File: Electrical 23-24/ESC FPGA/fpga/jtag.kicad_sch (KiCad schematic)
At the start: 0 parts

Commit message: idk but something
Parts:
- added J1: SBH11-PBPC-D07-ST-BK, programmer:SULLINS_SBH11-PBPC-D07-ST-BK, symbol programmer:SBH11-PBPC-D07-ST-BK
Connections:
- new net GND: J1.1, J1.11, J1.13, J1.3, J1.5, J1.7, J1.9
- new net TCK: J1.6
- new net TDI: J1.10
- new net TDO: J1.8
- new net TMS: J1.4
- new net VREF: J1.2
- no-connect marks 0 -> 2
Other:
- note added: "Due to the need of a programmer, it was decided that it was better to make one externally than on-board the chip This board includes a 14-pin 2.54mm header (the Xilinx Header is 2.00mm pitch)"
- note removed: "Due to the need of a programmer, it was decided that it was better to make one externally than on-board the chip"
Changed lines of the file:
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@@
 (kicad_sch (version 20230121) (generator eeschema)
   (paper "A4")
-  (text "Due to the need of a programmer, it was decided that it\nwas better to make one externally than on-board the chip"
-    (at 19.05 26.67 0)
+  (junction (at 127 91.44) (diameter 0) (color 0 0 0 0)
+  )
+  (junction (at 127 96.52) (diameter 0) (color 0 0 0 0)
+  )
+  (junction (at 127 104.14) (diameter 0) (color 0 0 0 0)
+  )
+  (junction (at 127 99.06) (diameter 0) (color 0 0 0 0)
+  )
+  (junction (at 127 101.6) (diameter 0) (color 0 0 0 0)
+  )
+  (junction (at 127 93.98) (diameter 0) (color 0 0 0 0)
+  )
+  (no_connect (at 152.4 101.6))
+  (no_connect (at 152.4 104.14))
+  (wire (pts (xy 127 91.44) (xy 127 93.98))
+    (stroke (width 0) (type default))
+  )
+  (wire (pts (xy 127 96.52) (xy 127 99.06))
+    (stroke (width 0) (type default))
+  )
+  (wire (pts (xy 127 88.9) (xy 127 91.44))
+    (stroke (width 0) (type default))
+  )
+  (wire (pts (xy 127 101.6) (xy 127 104.14))
+    (stroke (width 0) (type default))
+  )
+  (wire (pts (xy 127 93.98) (xy 127 96.52))
+    (stroke (width 0) (type default))
+  )
+  (wire (pts (xy 127 104.14) (xy 127 105.41))
+    (stroke (width 0) (type default))
+  )
+  (wire (pts (xy 127 99.06) (xy 127 101.6))
+    (stroke (width 0) (type default))
+  )
+  (text "Due to the need of a programmer, it was decided that it\nwas better to make one externally than on-board the chip\n\nThis board includes a 14-pin 2.54mm header\n(the Xilinx Header is 2.00mm pitch)"
+    (at 19.05 36.83 0)
     (effects (font (size 2.54 2.54)) (justify left bottom))
   )
+  (global_label "TDO" (shape input) (at 152.4 96.52 0) (fields_autoplaced)
+    (effects (font (size 1.27 1.27)) (justify left))
+    (property "Intersheetrefs" "${INTERSHEET_REFS}" (at 158.9533 96.52 0)
+      (effects (font (size 1.27 1.27)) (justify left) hide)
+    )
+  )
+  (global_label "VREF" (shape input) (at 152.4 88.9 0) (fields_autoplaced)
+    (effects (font (size 1.27 1.27)) (justify left))
+    (property "Intersheetrefs" "${INTERSHEET_REFS}" (at 159.9814 88.9 0)
+      (effects (font (size 1.27 1.27)) (justify left) hide)
+    )
+  )
+  (global_label "TMS" (shape input) (at 152.4 91.44 0) (fields_autoplaced)
+    (effects (font (size 1.27 1.27)) (justify left))
+    (property "Intersheetrefs" "${INTERSHEET_REFS}" (at 159.0137 91.44 0)
+      (effects (font (size 1.27 1.27)) (justify left) hide)
+    )
+  )
+  (global_label "TCK" (shape input) (at 152.4 93.98 0) (fields_autoplaced)
+    (effects (font (size 1.27 1.27)) (justify left))
+    (property "Intersheetrefs" "${INTERSHEET_REFS}" (at 158.8928 93.98 0)
+      (effects (font (size 1.27 1.27)) (justify left) hide)
+    )
+  )
+  (global_label "TDI" (shape input) (at 152.4 99.06 0) (fields_autoplaced)
+    (effects (font (size 1.27 1.27)) (justify left))
+    (property "Intersheetrefs" "${INTERSHEET_REFS}" (at 158.2276 99.06 0)
+      (effects (font (size 1.27 1.27)) (justify left) hide)
+    )
+  )
+  (symbol (lib_id "programmer:SBH11-PBPC-D07-ST-BK") (at 139.7 96.52 0) (unit 1)
+    (in_bom yes) (on_board yes) (dnp no) (fields_autoplaced)
+    (property "Reference" "J1" (at 139.7 81.28 0)
+      (effects (font (size 1.27 1.27)))
+    )
+    (property "Value" "SBH11-PBPC-D07-ST-BK" (at 139.7 83.82 0)
+      (effects (font (size 1.27 1.27)))
+    )
+    (property "Footprint" "programmer:SULLINS_SBH11-PBPC-D07-ST-BK" (at 139.7 96.52 0)
+      (effects (font (size 1.27 1.27)) (justify bottom) hide)
+    )
+    (property "Datasheet" "" (at 139.7 96.52 0)
+      (effects (font (size 1.27 1.27)) hide)
+    )
+    (property "PARTREV" "J" (at 139.7 96.52 0)
+      (effects (font (size 1.27 1.27)) (justify bottom) hide)
+    )
+    (property "STANDARD" "Manufacturer Recommendation" (at 139.7 96.52 0)
+      (effects (font (size 1.27 1.27)) (justify bottom) hide)
+    )
+    (property "MANUFACTURER" "Sullins" (at 139.7 96.52 0)
+      (effects (font (size 1.27 1.27)) (justify bottom) hide)
+    )
+    (pin "1")
+    (pin "10")
+    (pin "11")
+    (pin "12")
+    (pin "13")
+    (pin "14")
+    (pin "2")
+    (pin "3")
+    (pin "4")
+    (pin "5")
+    (pin "6")
+    (pin "7")
+    (pin "8")
+    (pin "9")
+    (instances
+      (project "fpga"
+        (path "/5bf59577-a814-4364-8f7a-37815cfb5474/3d3d8e49-9c73-4011-93e8-c0355c1f458a"
+          (reference "J1") (unit 1)
+        )
+      )
+    )
+  )
+  (symbol (lib_id "power:GND") (at 127 105.41 0) (unit 1)
+    (in_bom yes) (on_board yes) (dnp no) (fields_autoplaced)
+    (property "Reference" "#PWR09" (at 127 111.76 0)
+      (effects (font (size 1.27 1.27)) hide)
+    )
+    (property "Value" "GND" (at 127 110.49 0)
+      (effects (font (size 1.27 1.27)))
+    )
+    (property "Footprint" "" (at 127 105.41 0)
+      (effects (font (size 1.27 1.27)) hide)
+    )
+    (property "Datasheet" "" (at 127 105.41 0)
+      (effects (font (size 1.27 1.27)) hide)
+    )
+    (pin "1")
+    (instances
+      (project "fpga"
+        (path "/5bf59577-a814-4364-8f7a-37815cfb5474/3d3d8e49-9c73-4011-93e8-c0355c1f458a"
+          (reference "#PWR09") (unit 1)
+        )
+      )
+    )
+  )
 )

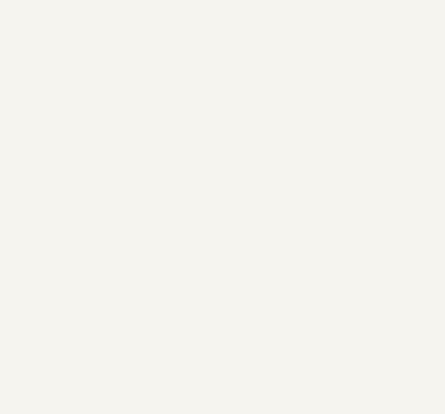
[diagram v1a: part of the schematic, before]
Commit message: Add fpga stuff and stencils
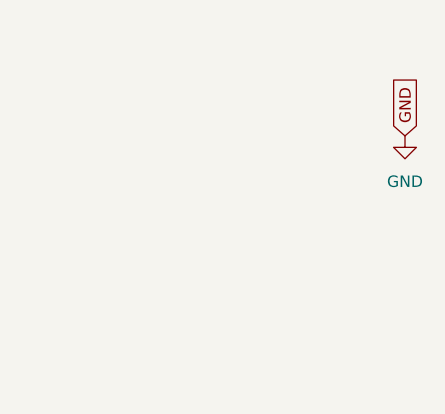
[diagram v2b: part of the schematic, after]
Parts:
- J1: Digi (none) -> https://www.digikey.com/en/products/detail/sullins-connecto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
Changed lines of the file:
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@@
+    )
+  )
+  (global_label "GND" (shape input) (at 273.05 29.21 90) (fields_autoplaced)
+    (effects (font (size 1.27 1.27)) (justify left))
+    (property "Intersheetrefs" "${INTERSHEET_REFS}" (at 273.05 22.3543 90)
+      (effects (font (size 1.27 1.27)) (justify left) hide)
     )
   )
@@
     )
   )
+  (symbol (lib_id "power:GND") (at 273.05 29.21 0) (unit 1)
+    (in_bom yes) (on_board yes) (dnp no) (fields_autoplaced)
+    (property "Reference" "#PWR016" (at 273.05 35.56 0)
+      (effects (font (size 1.27 1.27)) hide)
+    )
+    (property "Value" "GND" (at 273.05 34.29 0)
+      (effects (font (size 1.27 1.27)))
+    )
+    (property "Footprint" "" (at 273.05 29.21 0)
+      (effects (font (size 1.27 1.27)) hide)
+    )
+    (property "Datasheet" "" (at 273.05 29.21 0)
+      (effects (font (size 1.27 1.27)) hide)
+    )
+    (pin "1")
+    (instances
+      (project "fpga"
+        (path "/5bf59577-a814-4364-8f7a-37815cfb5474/3e04db34-3f8a-4742-be82-6fa24c009343"
+          (reference "#PWR016") (unit 1)
+        )
+        (path "/5bf59577-a814-4364-8f7a-37815cfb5474/1f83b38b-56ef-4110-879b-13379f9dd920"
+          (reference "#PWR026") (unit 1)
+        )
+        (path "/5bf59577-a814-4364-8f7a-37815cfb5474/a286b274-4434-47ab-983d-e64806fdcbd6"
+          (reference "#PWR036") (unit 1)
+        )
+        (path "/5bf59577-a814-4364-8f7a-37815cfb5474/3d3d8e49-9c73-4011-93e8-c0355c1f458a"
+          (reference "#PWR042") (unit 1)
+        )
+      )
+    )
+  )
   (symbol (lib_id "programmer:SBH11-PBPC-D07-ST-BK") (at 139.7 96.52 0) (unit 1)
     (in_bom yes) (on_board yes) (dnp no) (fields_autoplaced)
@@
       (effects (font (size 1.27 1.27)) (justify bottom) hide)
     )
+    (property "Digi" "https://www.digikey.com/en/products/detail/sullins-connector-solutions/sbh11-pbpc-d07-st-bk/1990063" (at 139.7 96.52 0)
+      (effects (font (size 1.27 1.27)) hide)
+    )
     (pin "1")
